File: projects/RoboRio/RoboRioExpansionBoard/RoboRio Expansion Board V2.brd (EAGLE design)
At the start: 56.6 x 77.5 mm, 136 parts, among them J1 RRINTERFACE-FEMALE, J10 SPI_MISO, J11 SPI_MOSI, J12 I2C_SCL, J13 I2C_SDA, J14 UART_TX, J15 UART_RX, J16 LCD, J17 ADC1, J18 ADC2, J19 ADC3, J2 MICROSD-HINGED, J20 ADC4, J21 ADC5, J22 ADC6, J23 ADC7, J25 PWM0, J26 PWM1, J27 PWM2, J28 PWM3, J29 PWM4, J3 51387-0578, J30 PWM5, J31 PWM6, J32 PWM7, J33 PWM8, J34 PWM9, J35 AI0, J36 AI1, J37 AI2, J38 AI3, J39 AO0, J4 GPIO0, J40 AO1, J5 GPIO1, J6 GPIO2, J7 GPIO3, J8 SPI_CS, J9 SPI_CLK, Q1 NPN-SOT416, Q2 NPN-SOT416, Q3 NPN-SOT416, SW1 450-1781-ND, U1 FTS31XS-U, U2 74LVC1G126DCK, U3 24LC256ST, U4 REG1117, U5 TPS2115APWR, U6 P8X32A-Q44_P, U7 TC54VN43, U8 ADC124S01, U9 ADC124S01, Y1 5MHz

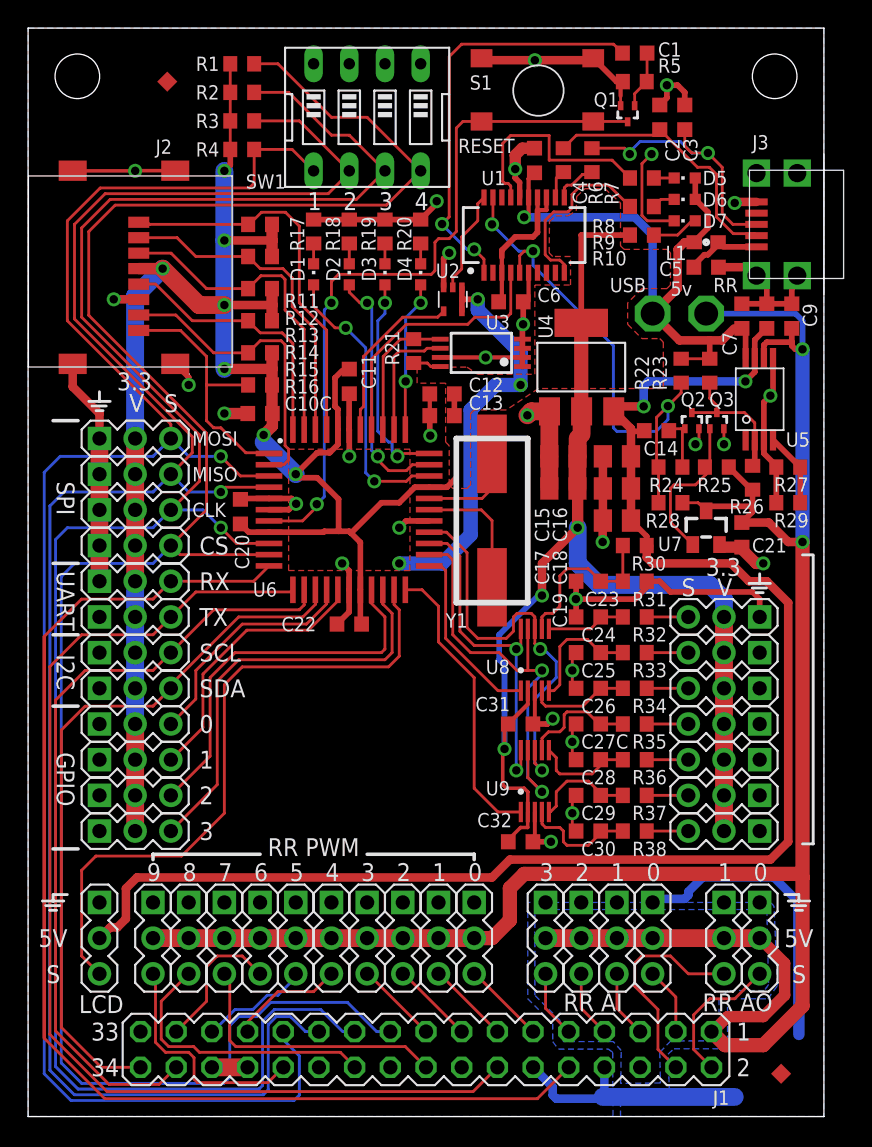
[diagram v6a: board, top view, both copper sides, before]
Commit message: Minor trace updates
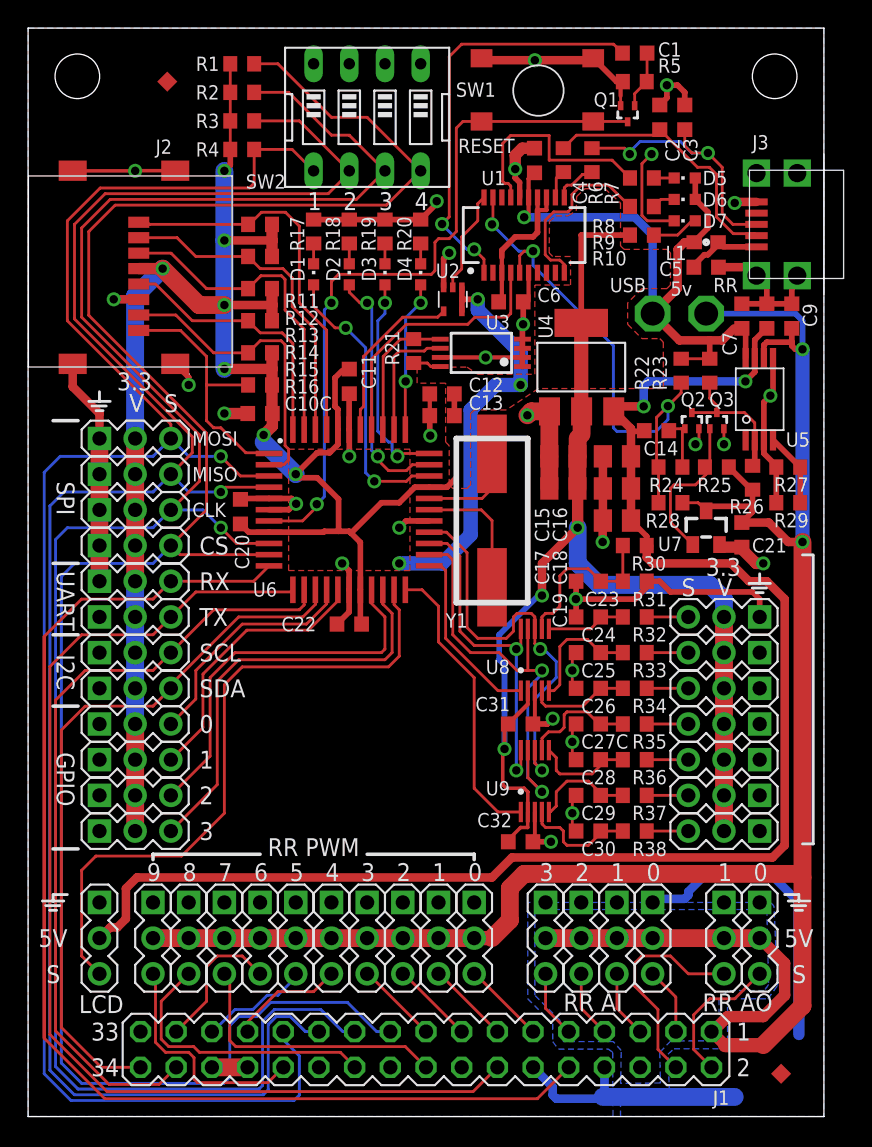
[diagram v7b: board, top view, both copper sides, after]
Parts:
- removed S1: RESETBUTTON9001DEFAULT, resetbutton9001:RESETBUTTON9001
- added SW2: 450-1781-ND, crystalsmt:EDG-04
- L1: value FERRITE BEAD!!! -> MPZ1608S221ATA00
- SW1: value 450-1781-ND -> RESETBUTTON9001DEFAULT; device crystalsmt:EDG-04 -> resetbutton9001:RESETBUTTON9001
- U1: value FTS31XS-U -> FT231XS-R
- U2: value 74LVC1G126DCK -> 74LVC1G126SE-7
- U4: value REG1117 -> AP1117E33G-13
- U8, U9: value ADC124S01 -> ADC124S021
- moved SW1 12.3 mm to (36.3, 73.0)
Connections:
- net N$6 renamed TX_LED#
- net N$7 renamed RX_LED#
- net !RESET: now also SW1.1, SW1.2; no longer S1.1, S1.2
- net DGND: now also SW2.1, SW2.2, SW2.3, SW2.4; no longer S1.3, S1.4, SW1.1, SW1.2
- net IO6: now also SW2.5; no longer SW1.5
- net IO7: now also SW2.6; no longer SW1.6
- net IO8: now also SW2.7; no longer SW1.7
- net IO9: now also SW2.8; no longer SW1.8

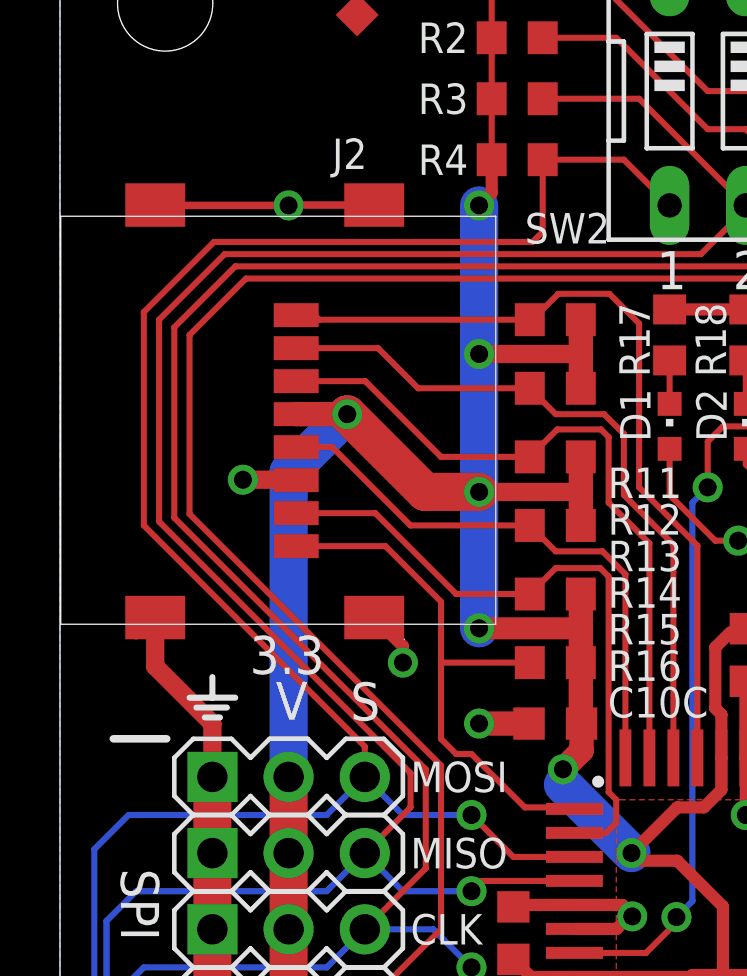
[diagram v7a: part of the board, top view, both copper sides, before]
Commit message: Sd Card package fixed
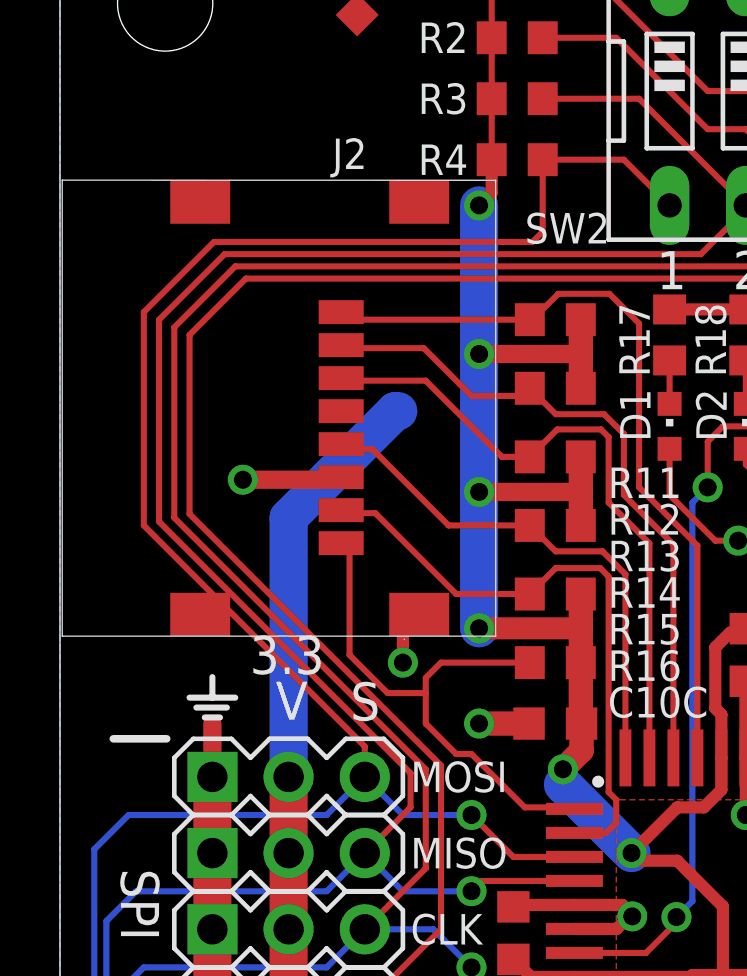
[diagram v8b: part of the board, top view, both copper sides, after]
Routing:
- net DGND: track 227.8 -> 215.7 mm, vias 30 -> 29
- net +3V3: track 257.6 -> 251.3 mm, vias 13 -> 12
- net IO2: track 23.2 -> 21.7 mm
- net IO5: track 21.9 -> 20.4 mm
- net IO0: track 27.5 -> 26.2 mm
- net IO1: track 23.6 -> 22.3 mm
- net IO3: track 19.2 -> 18.1 mm
